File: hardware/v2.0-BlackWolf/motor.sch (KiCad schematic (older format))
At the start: 11 parts, among them M1 MOTOR_MOUNTS_AND_ENCODERS, M2 LEFT_MOTOR, M4 RIGHT_MOTOR, U2 MAX14871, U3 MAX14871

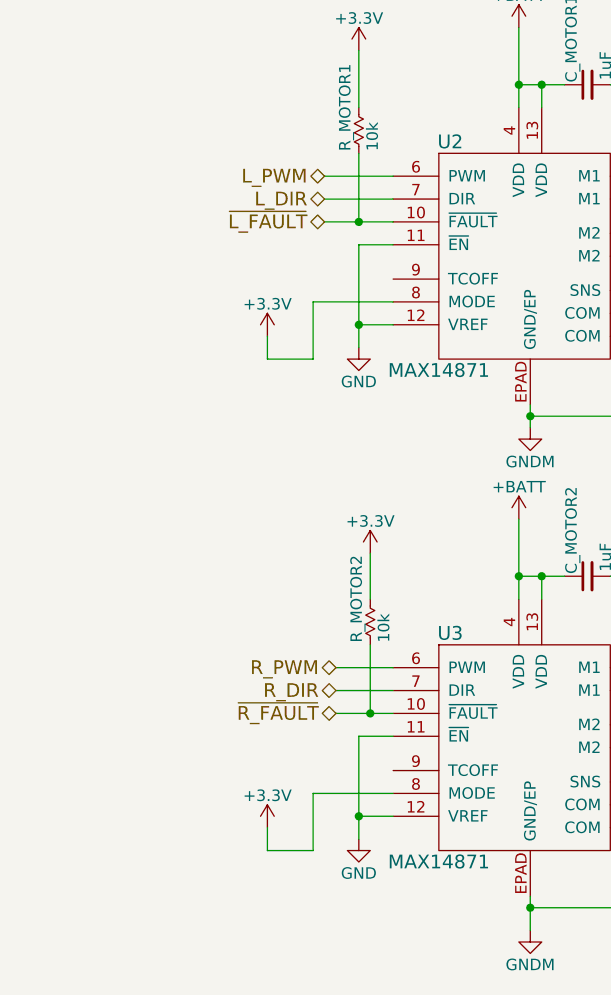
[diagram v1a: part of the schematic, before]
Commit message: PCB: Fixed floating PWM output problem
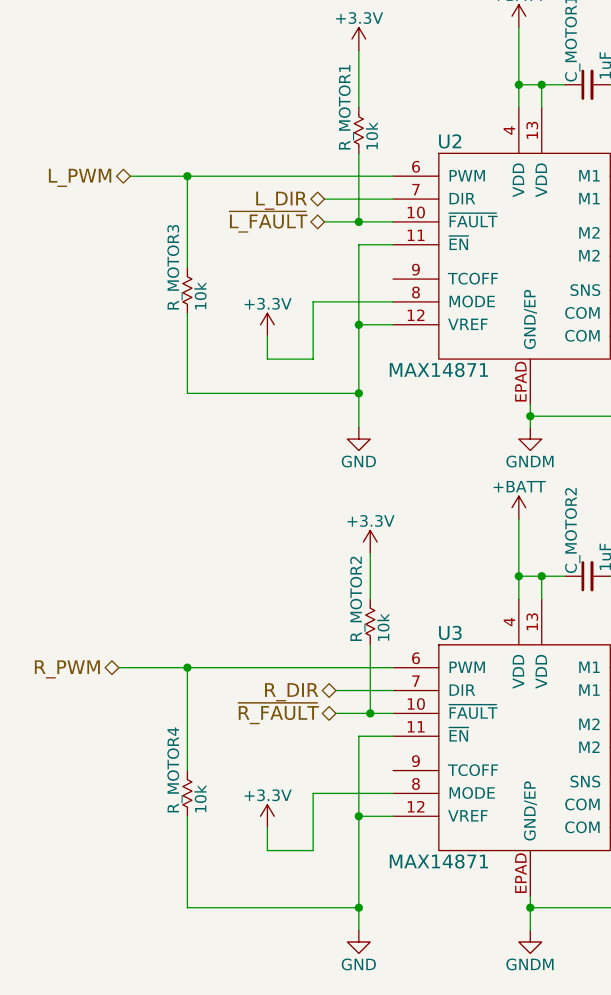
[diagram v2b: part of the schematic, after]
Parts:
- added R_MOTOR3, R_MOTOR4: 10k, Resistors_SMD:R_0603, symbol R_Small
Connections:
- net GND: now also R_MOTOR3.2, R_MOTOR4.2
- net L_PWM: now also R_MOTOR3.1
- net R_PWM: now also R_MOTOR4.1
